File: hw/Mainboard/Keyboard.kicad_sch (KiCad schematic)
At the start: 6 parts, among them J2 KEYBOARD, U1 74LS145

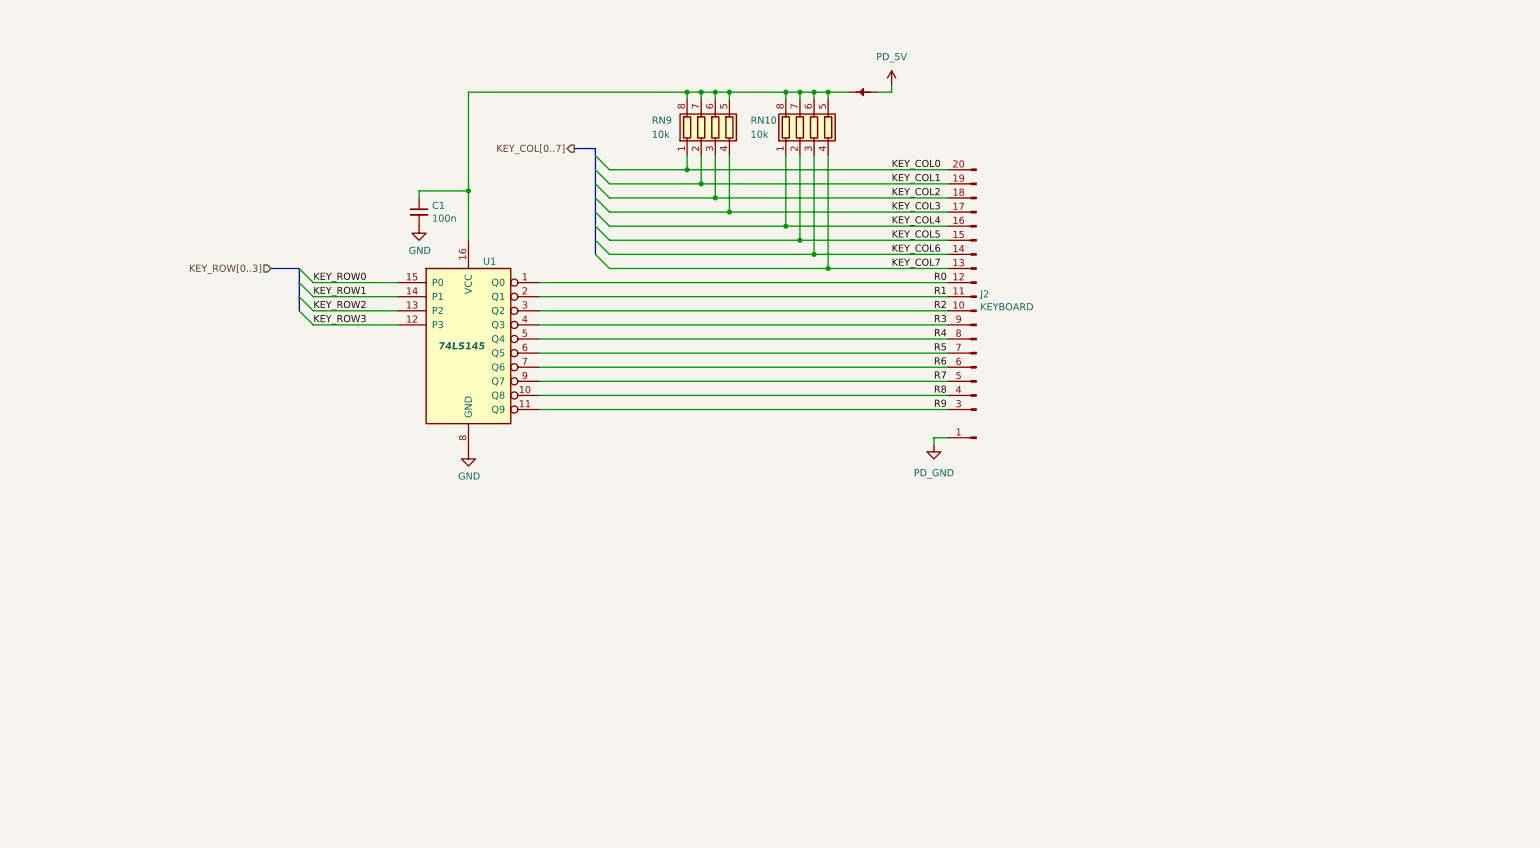
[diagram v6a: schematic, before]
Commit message: hw: tidy audio, cass, IEEE, keyboard, magic, user
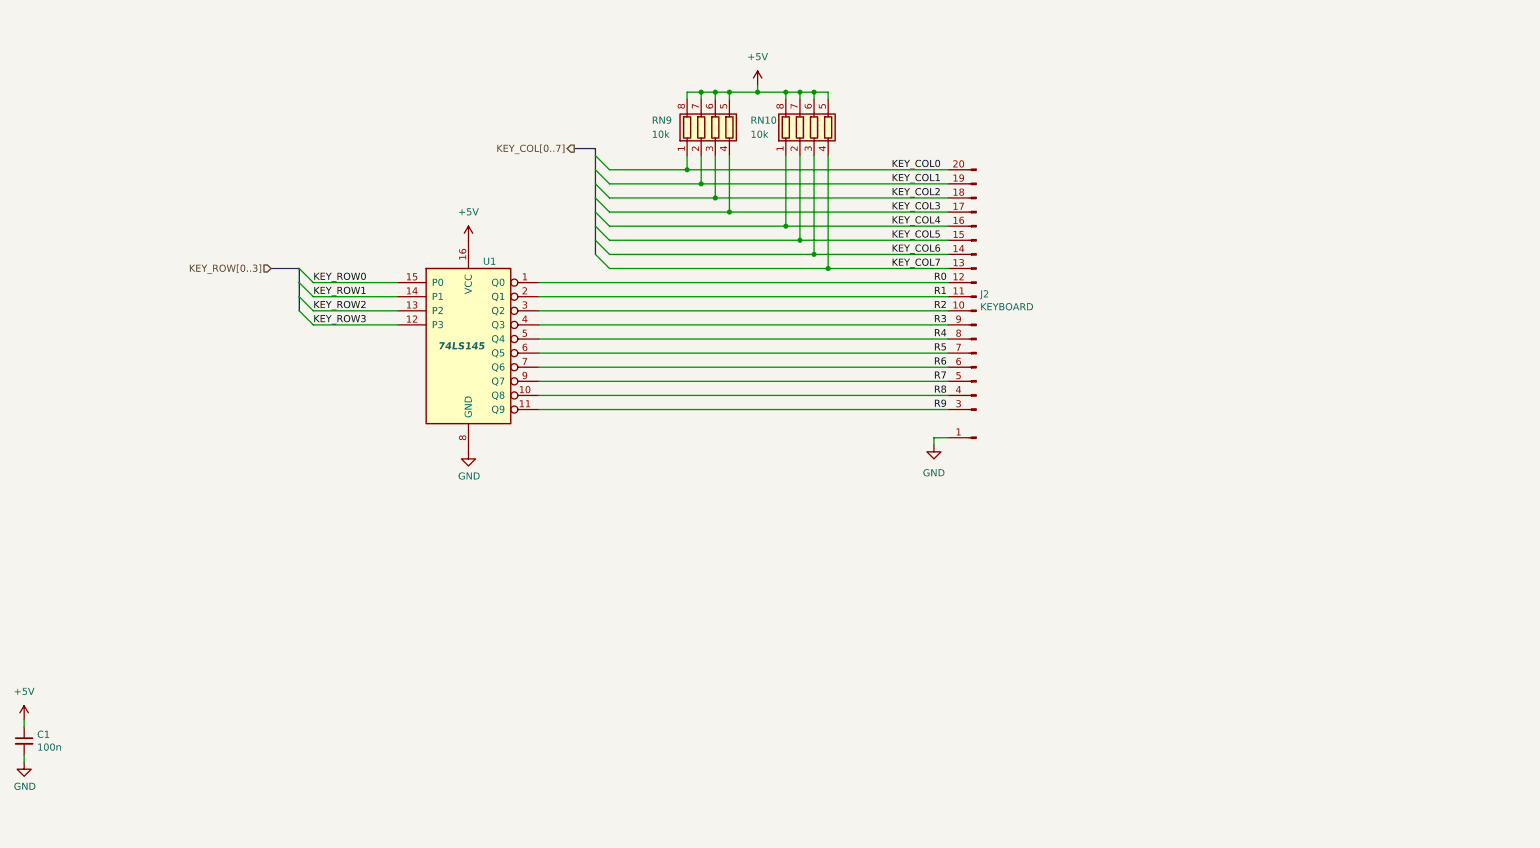
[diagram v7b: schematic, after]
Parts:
- removed NT35: +5V, PET:NetTie-2_SMD_Pad_1.6_to_0.4mm, symbol PET:PowerTie_2
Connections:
- net PD_GND is gone; now on net GND: J2.1 (Pin_1)
- net +5V: now reaches C1.1, RN10.5 (R4.2), RN10.6 (R3.2), RN10.7 (R2.2), RN10.8 (R1.2), RN9.5 (R4.2), RN9.6 (R3.2), RN9.7 (R2.2), RN9.8 (R1.2), U1.16 (VCC)
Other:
- moved on the sheet: C1
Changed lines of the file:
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@@
   (junction (at 157.48 66.04) (diameter 0) (color 0 0 0 0)
   )
-  (junction (at 110.49 83.82) (diameter 0) (color 0 0 0 0)
+  (junction (at 162.56 66.04) (diameter 0) (color 0 0 0 0)
   )
   (junction (at 167.64 66.04) (diameter 0) (color 0 0 0 0)
@@
   (junction (at 175.26 97.79) (diameter 0) (color 0 0 0 0)
   )
-  (junction (at 175.26 66.04) (diameter 0) (color 0 0 0 0)
-  )
   (junction (at 157.48 87.63) (diameter 0) (color 0 0 0 0)
   )
@@
   (junction (at 170.18 66.04) (diameter 0) (color 0 0 0 0)
   )
-  (junction (at 149.86 66.04) (diameter 0) (color 0 0 0 0)
-  )
   (junction (at 172.72 95.25) (diameter 0) (color 0 0 0 0)
   )
@@
     (stroke (width 0) (type default) (color 0 0 0 0))
   )
+  (wire (pts (xy 162.56 64.77) (xy 162.56 66.04))
+    (stroke (width 0) (type default) (color 0 0 0 0))
+  )
   (wire (pts (xy 196.85 128.27) (xy 194.31 128.27))
     (stroke (width 0) (type default) (color 0 0 0 0))
@@
     (stroke (width 0) (type default) (color 0 0 0 0))
   )
-  (wire (pts (xy 110.49 83.82) (xy 110.49 92.71))
-    (stroke (width 0) (type default) (color 0 0 0 0))
-  )
   (wire (pts (xy 135.89 92.71) (xy 170.18 92.71))
     (stroke (width 0) (type default) (color 0 0 0 0))
@@
     (stroke (width 0) (type default) (color 0 0 0 0))
   )
-  (wire (pts (xy 175.26 66.04) (xy 179.07 66.04))
-    (stroke (width 0) (type default) (color 0 0 0 0))
-  )
   (wire (pts (xy 135.89 85.09) (xy 154.94 85.09))
     (stroke (width 0) (type default) (color 0 0 0 0))
@@
     (stroke (width 0) (type default) (color 0 0 0 0))
   )
-  (wire (pts (xy 101.6 83.82) (xy 110.49 83.82))
-    (stroke (width 0) (type default) (color 0 0 0 0))
-  )
   (wire (pts (xy 157.48 66.04) (xy 157.48 67.31))
     (stroke (width 0) (type default) (color 0 0 0 0))
   )
-  (wire (pts (xy 186.69 64.77) (xy 186.69 66.04))
-    (stroke (width 0) (type default) (color 0 0 0 0))
-  )
   (wire (pts (xy 135.89 97.79) (xy 175.26 97.79))
     (stroke (width 0) (type default) (color 0 0 0 0))
@@
     (stroke (width 0) (type default) (color 0 0 0 0))
   )
-  (wire (pts (xy 149.86 66.04) (xy 110.49 66.04))
-    (stroke (width 0) (type default) (color 0 0 0 0))
-  )
   (wire (pts (xy 123.19 105.41) (xy 196.85 105.41))
     (stroke (width 0) (type default) (color 0 0 0 0))
@@
     (stroke (width 0) (type default) (color 0 0 0 0))
   )
-  (wire (pts (xy 186.69 66.04) (xy 184.15 66.04))
-    (stroke (width 0) (type default) (color 0 0 0 0))
-  )
   (wire (pts (xy 123.19 113.03) (xy 196.85 113.03))
     (stroke (width 0) (type default) (color 0 0 0 0))
   )
-  (wire (pts (xy 101.6 85.09) (xy 101.6 83.82))
+  (wire (pts (xy 30.48 180.34) (xy 30.48 179.07))
     (stroke (width 0) (type default) (color 0 0 0 0))
   )
@@
     (stroke (width 0) (type default) (color 0 0 0 0))
   )
-  (wire (pts (xy 110.49 66.04) (xy 110.49 83.82))
+  (wire (pts (xy 30.48 186.69) (xy 30.48 185.42))
+    (stroke (width 0) (type default) (color 0 0 0 0))
+  )
+  (wire (pts (xy 162.56 66.04) (xy 167.64 66.04))
     (stroke (width 0) (type default) (color 0 0 0 0))
   )
@@
     (stroke (width 0) (type default) (color 0 0 0 0))
   )
-  (wire (pts (xy 157.48 66.04) (xy 167.64 66.04))
+  (wire (pts (xy 157.48 66.04) (xy 162.56 66.04))
     (stroke (width 0) (type default) (color 0 0 0 0))
   )
@@
     (pin "9")
   )
-  (symbol (lib_id "Device:C_Small") (at 101.6 87.63 0) (unit 1)
-    (in_bom yes) (on_board yes)
-    (property "Reference" "C1" (id 0) (at 103.9368 86.4616 0)
+  (symbol (lib_id "Device:C_Small") (at 30.48 182.88 0) (unit 1)
+    (in_bom yes) (on_board yes)
+    (property "Reference" "C1" (id 0) (at 32.8168 181.7116 0)
       (effects (font (size 1.27 1.27)) (justify left))
     )
-    (property "Value" "100n" (id 1) (at 103.9368 88.773 0)
+    (property "Value" "100n" (id 1) (at 32.8168 184.023 0)
       (effects (font (size 1.27 1.27)) (justify left))
     )
-    (property "Footprint" "Capacitor_SMD:C_0402_1005Metric" (id 2) (at 101.6 87.63 0)
-      (effects (font (size 1.27 1.27)) hide)
-    )
-    (property "Datasheet" "https://datasheet.lcsc.com/lcsc/1810191219_Samsung-Electro-Mechanics-CL05B104KO5NNNC_C1525.pdf" (id 3) (at 101.6 87.63 0)
-      (effects (font (size 1.27 1.27)) hide)
-    )
-    (property "LCSC" "C1525" (id 4) (at 101.6 87.63 0)
+    (property "Footprint" "Capacitor_SMD:C_0402_1005Metric" (id 2) (at 30.48 182.88 0)
+      (effects (font (size 1.27 1.27)) hide)
+    )
+    (property "Datasheet" "https://datasheet.lcsc.com/lcsc/1810191219_Samsung-Electro-Mechanics-CL05B104KO5NNNC_C1525.pdf" (id 3) (at 30.48 182.88 0)
+      (effects (font (size 1.27 1.27)) hide)
+    )
+    (property "LCSC" "C1525" (id 4) (at 30.48 182.88 0)
       (effects (font (size 1.27 1.27)) hide)
     )
@@
     (pin "2")
   )
-  (symbol (lib_id "power:GND") (at 101.6 90.17 0) (unit 1)
-    (in_bom yes) (on_board yes)
-    (property "Reference" "#PWR03" (id 0) (at 101.6 96.52 0)
-      (effects (font (size 1.27 1.27)) hide)
-    )
-    (property "Value" "GND" (id 1) (at 101.727 94.5642 0))
-    (property "Footprint" "" (id 2) (at 101.6 90.17 0)
-      (effects (font (size 1.27 1.27)) hide)
-    )
-    (property "Datasheet" "" (id 3) (at 101.6 90.17 0)
-      (effects (font (size 1.27 1.27)) hide)
-    )
-    (pin "1")
-  )
-  (symbol (lib_id "PET:PowerTie_2") (at 181.61 66.04 0) (mirror y) (unit 1)
+  (symbol (lib_id "power:GND") (at 30.48 186.69 0) (unit 1)
+    (in_bom yes) (on_board yes)
+    (property "Reference" "#PWR03" (id 0) (at 30.48 193.04 0)
+      (effects (font (size 1.27 1.27)) hide)
+    )
+    (property "Value" "GND" (id 1) (at 30.607 191.0842 0))
+    (property "Footprint" "" (id 2) (at 30.48 186.69 0)
+      (effects (font (size 1.27 1.27)) hide)
+    )
+    (property "Datasheet" "" (id 3) (at 30.48 186.69 0)
+      (effects (font (size 1.27 1.27)) hide)
+    )
+    (pin "1")
+  )
+  (symbol (lib_id "power:+5V") (at 162.56 64.77 0) (unit 1)
     (in_bom yes) (on_board yes) (fields_autoplaced)
-    (property "Reference" "NT35" (id 0) (at 181.61 60.96 0)
-      (effects (font (size 1.27 1.27)) hide)
-    )
-    (property "Value" "+5V" (id 1) (at 181.61 63.5 0)
-      (effects (font (size 1.27 1.27)) hide)
-    )
-    (property "Footprint" "PET:NetTie-2_SMD_Pad_1.6_to_0.4mm" (id 2) (at 181.61 66.04 0)
-      (effects (font (size 1.27 1.27)) hide)
-    )
-    (property "Datasheet" "~" (id 3) (at 181.61 66.04 0)
-      (effects (font (size 1.27 1.27)) hide)
-    )
-    (pin "1")
-    (pin "2")
-  )
-  (symbol (lib_id "PET:PD_GND") (at 194.31 129.54 0) (unit 1)
+    (property "Reference" "#PWR?" (id 0) (at 162.56 68.58 0)
+      (effects (font (size 1.27 1.27)) hide)
+    )
+    (property "Value" "+5V" (id 1) (at 162.56 59.69 0))
+    (property "Footprint" "" (id 2) (at 162.56 64.77 0)
+      (effects (font (size 1.27 1.27)) hide)
+    )
+    (property "Datasheet" "" (id 3) (at 162.56 64.77 0)
+      (effects (font (size 1.27 1.27)) hide)
+    )
+    (pin "1")
+  )
+  (symbol (lib_id "power:+5V") (at 110.49 92.71 0) (unit 1)
     (in_bom yes) (on_board yes) (fields_autoplaced)
-    (property "Reference" "#PWR0166" (id 0) (at 194.31 135.89 0)
-      (effects (font (size 1.27 1.27)) hide)
-    )
-    (property "Value" "PD_GND" (id 1) (at 194.31 134.62 0))
-    (property "Footprint" "" (id 2) (at 194.31 129.54 0)
-      (effects (font (size 1.27 1.27)) hide)
-    )
-    (property "Datasheet" "" (id 3) (at 194.31 129.54 0)
+    (property "Reference" "#PWR?" (id 0) (at 110.49 96.52 0)
+      (effects (font (size 1.27 1.27)) hide)
+    )
+    (property "Value" "+5V" (id 1) (at 110.49 87.63 0))
+    (property "Footprint" "" (id 2) (at 110.49 92.71 0)
+      (effects (font (size 1.27 1.27)) hide)
+    )
+    (property "Datasheet" "" (id 3) (at 110.49 92.71 0)
+      (effects (font (size 1.27 1.27)) hide)
+    )
+    (pin "1")
+  )
+  (symbol (lib_id "power:+5V") (at 30.48 179.07 0) (unit 1)
+    (in_bom yes) (on_board yes) (fields_autoplaced)
+    (property "Reference" "#PWR?" (id 0) (at 30.48 182.88 0)
+      (effects (font (size 1.27 1.27)) hide)
+    )
+    (property "Value" "+5V" (id 1) (at 30.48 173.99 0))
+    (property "Footprint" "" (id 2) (at 30.48 179.07 0)
+      (effects (font (size 1.27 1.27)) hide)
+    )
+    (property "Datasheet" "" (id 3) (at 30.48 179.07 0)
       (effects (font (size 1.27 1.27)) hide)
     )
@@
     (pin "8")
   )
-  (symbol (lib_id "PET:PD_5V") (at 186.69 64.77 0) (unit 1)
-    (in_bom yes) (on_board yes) (fields_autoplaced)
-    (property "Reference" "#PWR0105" (id 0) (at 186.69 68.58 0)
-      (effects (font (size 1.27 1.27)) hide)
-    )
-    (property "Value" "PD_5V" (id 1) (at 186.69 59.69 0))
-    (property "Footprint" "" (id 2) (at 186.69 64.77 0)
-      (effects (font (size 1.27 1.27)) hide)
-    )
-    (property "Datasheet" "" (id 3) (at 186.69 64.77 0)
-      (effects (font (size 1.27 1.27)) hide)
-    )
-    (pin "1")
-  )
   (symbol (lib_id "Device:R_Pack04") (at 172.72 72.39 0) (unit 1)
     (in_bom yes) (on_board yes)
@@
     (pin "8")
   )
+  (symbol (lib_id "power:GND") (at 194.31 129.54 0) (unit 1)
+    (in_bom yes) (on_board yes) (fields_autoplaced)
+    (property "Reference" "#PWR?" (id 0) (at 194.31 135.89 0)
+      (effects (font (size 1.27 1.27)) hide)
+    )
+    (property "Value" "GND" (id 1) (at 194.31 134.62 0))
+    (property "Footprint" "" (id 2) (at 194.31 129.54 0)
+      (effects (font (size 1.27 1.27)) hide)
+    )
+    (property "Datasheet" "" (id 3) (at 194.31 129.54 0)
+      (effects (font (size 1.27 1.27)) hide)
+    )
+    (pin "1")
+  )
 )
